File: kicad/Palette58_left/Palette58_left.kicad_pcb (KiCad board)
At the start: 2 copper layers, 145 x 127.8 mm, 124 parts, among them SW1 MSK12C02-HB, SW2 TS-1187A-B-A-B

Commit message: Add mounting holes
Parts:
- added REF**: MountingHole_3.2mm_M3_Pad_Via, MountingHole:MountingHole_3.2mm_M3_Pad_Via, F.Cu at (87.0, -82.0)
- added REF**: MountingHole_3.2mm_M3_Pad_Via, MountingHole:MountingHole_3.2mm_M3_Pad_Via, F.Cu at (100.4, 0.00)
- added REF**: MountingHole_3.2mm_M3_Pad_Via, MountingHole:MountingHole_3.2mm_M3_Pad_Via, F.Cu at (13.5, 7.50)
- added REF**: MountingHole_3.2mm_M3_Pad_Via, MountingHole:MountingHole_3.2mm_M3_Pad_Via, F.Cu at (23.0, -77.5)
- LED1, LED10, LED11, LED12, LED13, LED14, LED15, LED16, LED17, LED18, LED19, LED2, LED20, LED21, LED22, LED23, LED24, LED25, LED26, LED27, LED28, LED29, LED3, LED4, LED5, LED6, LED7, LED8, LED9: value XINGLIGHTXL-1615RGBC-WS2812B -> (none); footprint LED_SMD:XINGLIGHT XL-1615RGBC-WS2812B -> WS2812B
- R1: footprint Resistor_SMD:R_0402_1005Metric -> Resistor
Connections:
- LED1 pad 1: VCC -> (no net)
- LED1 pad 2: Net-(LED1-DOUT) -> GND
- LED1 pad 3: GND -> (no net)
- LED1 pad 4: Net-(LED1-DIN) -> VCC
- LED10 pad 1: VCC -> (no net)
- LED10 pad 2: Net-(LED10-DOUT) -> GND
- LED10 pad 3: GND -> (no net)
- LED10 pad 4: Net-(LED10-DIN) -> VCC
- LED11 pad 1: VCC -> (no net)
- LED11 pad 2: Net-(LED11-DOUT) -> GND
- LED11 pad 3: GND -> (no net)
- LED11 pad 4: Net-(LED11-DIN) -> VCC
- LED12 pad 1: VCC -> (no net)
- LED12 pad 2: Net-(LED12-DOUT) -> GND
- LED12 pad 3: GND -> (no net)
- LED12 pad 4: Net-(LED12-DIN) -> VCC
- LED13 pad 1: VCC -> (no net)
- LED13 pad 2: Net-(LED13-DOUT) -> GND
- LED13 pad 3: GND -> (no net)
- LED13 pad 4: Net-(LED13-DIN) -> VCC
- LED14 pad 1: VCC -> (no net)
- LED14 pad 2: Net-(LED10-DIN) -> GND
- LED14 pad 3: GND -> (no net)
- LED14 pad 4: Net-(LED14-DIN) -> VCC
- LED15 pad 1: VCC -> (no net)
- LED15 pad 2: Net-(LED15-DOUT) -> GND
- LED15 pad 3: GND -> (no net)
- LED15 pad 4: Net-(LED11-DOUT) -> VCC
- LED16 pad 1: VCC -> (no net)
- LED16 pad 2: Net-(LED12-DIN) -> GND
- LED16 pad 3: GND -> (no net)
- LED16 pad 4: Net-(LED16-DIN) -> VCC
- LED17 pad 1: VCC -> (no net)
- LED17 pad 2: Net-(LED17-DOUT) -> GND
- LED17 pad 3: GND -> (no net)
- LED17 pad 4: Net-(LED13-DOUT) -> VCC
- LED18 pad 1: VCC -> (no net)
- LED18 pad 2: Net-(LED14-DIN) -> GND
- LED18 pad 3: GND -> (no net)
- LED18 pad 4: Net-(LED18-DIN) -> VCC
- LED19 pad 1: VCC -> (no net)
- LED19 pad 2: Net-(LED19-DOUT) -> GND
- LED19 pad 3: GND -> (no net)
- LED19 pad 4: Net-(LED15-DOUT) -> VCC
- LED2 pad 1: VCC -> (no net)
- LED2 pad 2: Net-(LED1-DIN) -> GND
- LED2 pad 3: GND -> (no net)
- LED2 pad 4: Net-(LED2-DIN) -> VCC
- LED20 pad 1: VCC -> (no net)
- LED20 pad 2: Net-(LED16-DIN) -> GND
- LED20 pad 3: GND -> (no net)
- LED20 pad 4: Net-(LED20-DIN) -> VCC
- LED21 pad 1: VCC -> (no net)
- LED21 pad 2: Net-(LED21-DOUT) -> GND
- LED21 pad 3: GND -> (no net)
- LED21 pad 4: Net-(LED17-DOUT) -> VCC
- LED22 pad 1: VCC -> (no net)
- LED22 pad 2: Net-(LED18-DIN) -> GND
- LED22 pad 3: GND -> (no net)
- LED22 pad 4: Net-(LED22-DIN) -> VCC
- LED23 pad 1: VCC -> (no net)
- LED23 pad 2: Net-(LED22-DIN) -> GND
- LED23 pad 3: GND -> (no net)
- LED23 pad 4: Net-(LED19-DOUT) -> VCC
- LED24 pad 1: VCC -> (no net)
- LED24 pad 2: Net-(LED20-DIN) -> GND
- LED24 pad 3: GND -> (no net)
- LED24 pad 4: Net-(LED24-DIN) -> VCC
- LED25 pad 1: VCC -> (no net)
- LED25 pad 2: Net-(LED25-DOUT) -> GND
- LED25 pad 3: GND -> (no net)
- LED25 pad 4: Net-(LED21-DOUT) -> VCC
- LED26 pad 1: VCC -> (no net)
- LED26 pad 2: Net-(LED26-DOUT) -> GND
- LED26 pad 3: GND -> (no net)
- LED26 pad 4: Net-(LED25-DOUT) -> VCC
- LED27 pad 1: VCC -> (no net)
- LED27 pad 2: Net-(LED27-DOUT) -> GND
- LED27 pad 3: GND -> (no net)
- LED27 pad 4: Net-(LED26-DOUT) -> VCC
- LED28 pad 1: VCC -> (no net)
- LED28 pad 2: Net-(LED28-DOUT) -> GND
- LED28 pad 3: GND -> (no net)
- LED28 pad 4: Net-(LED27-DOUT) -> VCC
- LED29 pad 1: VCC -> (no net)
- LED29 pad 2: unconnected-(LED29-DOUT-Pad2) -> GND
- LED29 pad 3: GND -> (no net)
- LED29 pad 4: Net-(LED28-DOUT) -> VCC
- LED3 pad 1: VCC -> (no net)
- LED3 pad 2: Net-(LED3-DOUT) -> GND
- LED3 pad 3: GND -> (no net)
- LED3 pad 4: Net-(LED3-DIN) -> VCC
- LED4 pad 1: VCC -> (no net)
- LED4 pad 2: Net-(LED3-DIN) -> GND
- LED4 pad 3: GND -> (no net)
- LED4 pad 4: Net-(LED4-DIN) -> VCC
- LED5 pad 1: VCC -> (no net)
- LED5 pad 2: Net-(LED5-DOUT) -> GND
- LED5 pad 3: GND -> (no net)
- LED5 pad 4: Net-(LED1-DOUT) -> VCC
- LED6 pad 1: VCC -> (no net)
- LED6 pad 2: Net-(LED2-DIN) -> GND
- LED6 pad 3: GND -> (no net)
- LED6 pad 4: Net-(LED10-DOUT) -> VCC
- LED7 pad 1: VCC -> (no net)
- LED7 pad 2: Net-(LED11-DIN) -> GND
- LED7 pad 3: GND -> (no net)
- LED7 pad 4: Net-(LED3-DOUT) -> VCC
- LED8 pad 1: VCC -> (no net)
- LED8 pad 2: Net-(LED4-DIN) -> GND
- LED8 pad 3: GND -> (no net)
- LED8 pad 4: Net-(LED12-DOUT) -> VCC
- LED9 pad 1: VCC -> (no net)
- LED9 pad 2: Net-(LED13-DIN) -> GND
- LED9 pad 3: GND -> (no net)
- LED9 pad 4: Net-(LED5-DOUT) -> VCC
- R1 pad 1: Net-(LED24-DIN) -> (no net)
- R1 pad 2: P0.06 -> (no net)
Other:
- net class Default added: clearance 0.2, trace_width 0.25, via_dia 0.8, via_drill 0.4

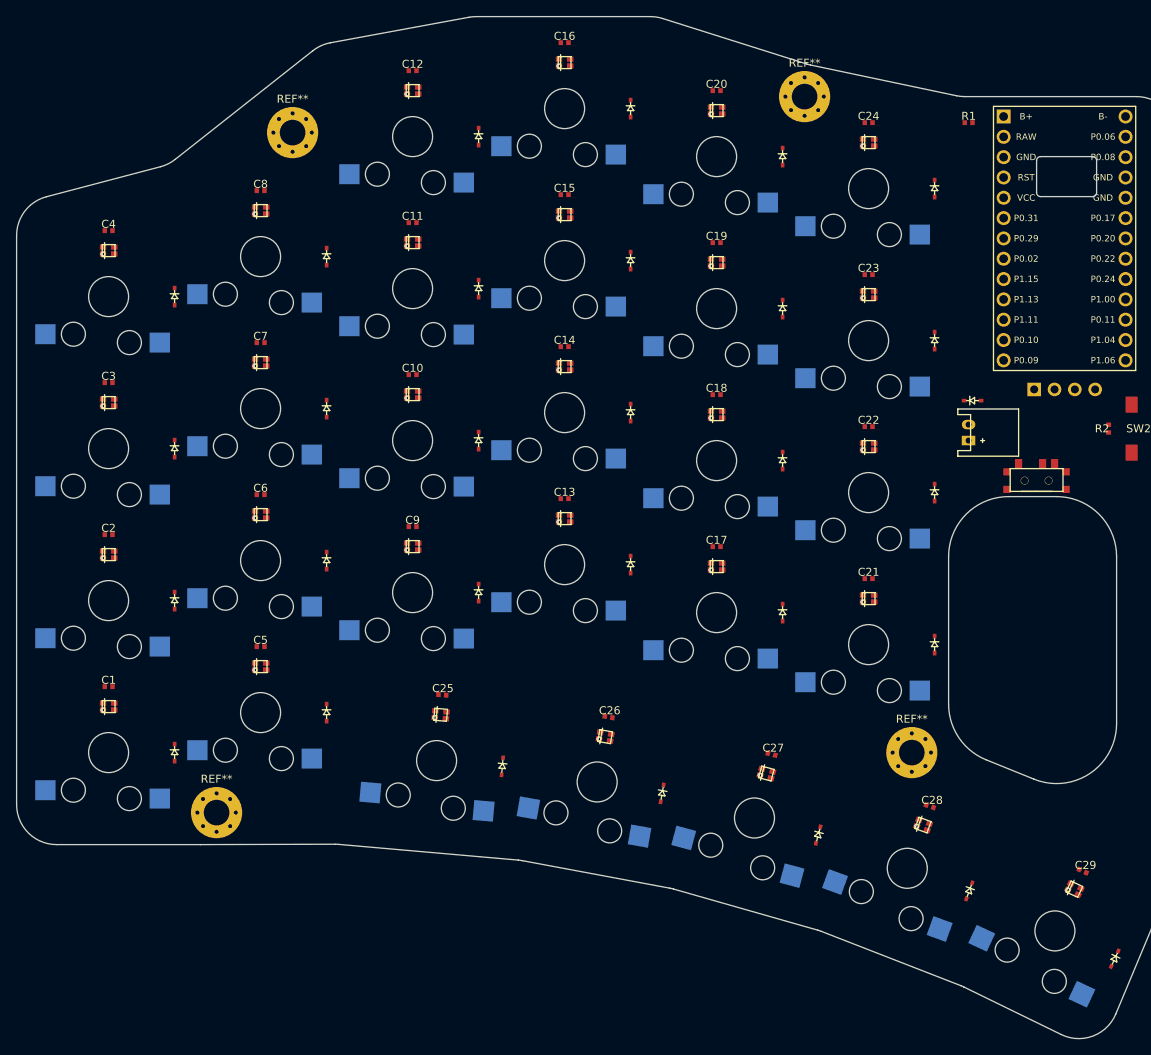
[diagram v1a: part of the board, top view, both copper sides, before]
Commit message: Add tooling holes
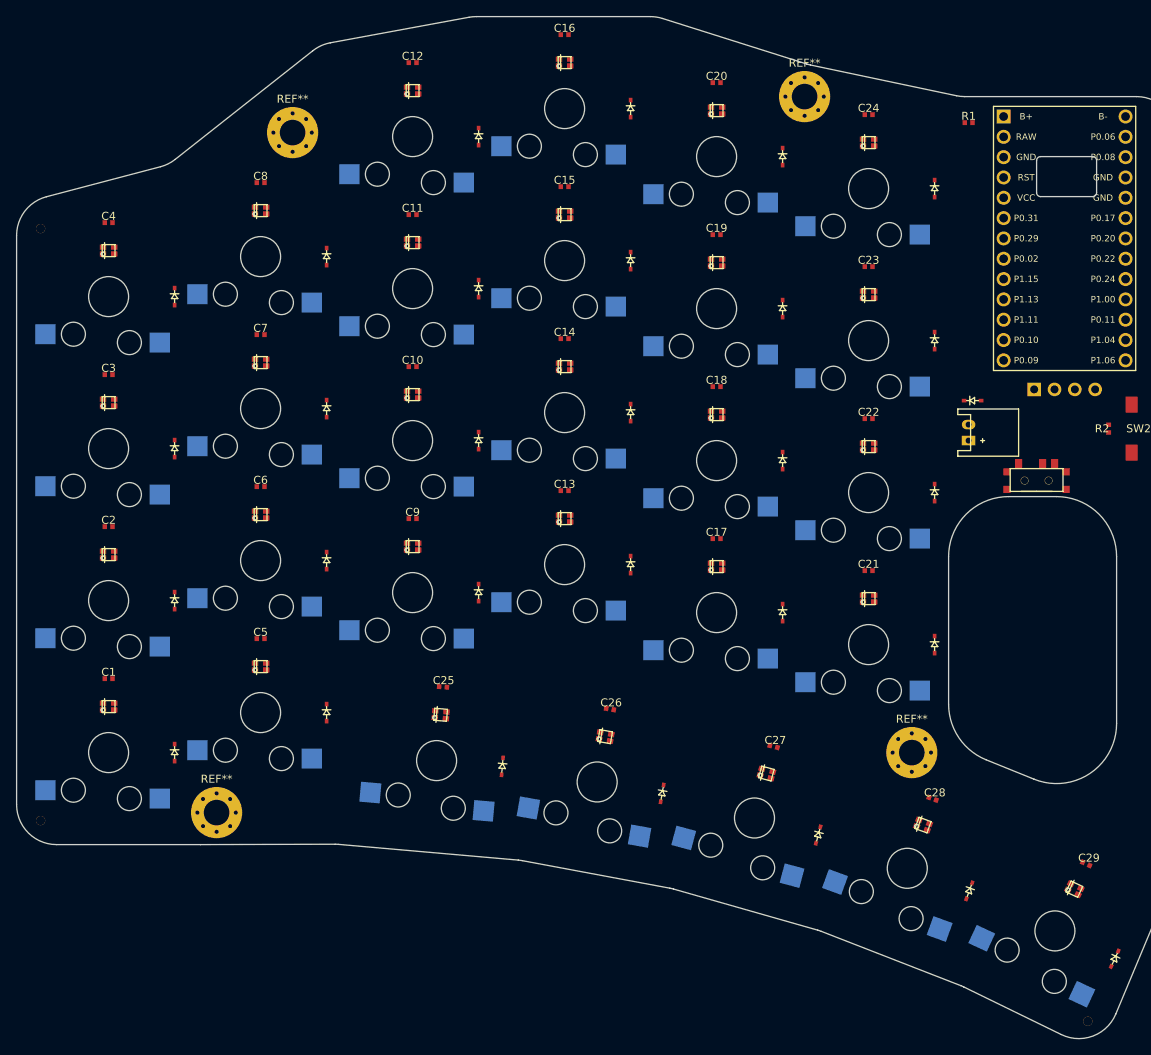
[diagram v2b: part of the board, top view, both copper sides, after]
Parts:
- added _34: , ToolingHole, F.Cu at (-8.50, -65.5)
- added _35: , ToolingHole, F.Cu at (-8.50, 8.50)
- added _36: , ToolingHole, F.Cu at (122.4, 33.6)
- moved C1 1.00 mm to (0.00, -9.25)
- moved C10 1.00 mm to (38.0, -48.2)
- moved C11 1.00 mm to (38.0, -67.2)
- moved C12 1.00 mm to (38.0, -86.2)
- moved C13 1.00 mm to (57.0, -32.8)
- moved C14 1.00 mm to (57.0, -51.8)
- moved C15 1.00 mm to (57.0, -70.8)
- moved C16 1.00 mm to (57.0, -89.8)
- moved C17 1.00 mm to (76.0, -26.8)
- moved C18 1.00 mm to (76.0, -45.8)
- moved C19 1.00 mm to (76.0, -64.8)
- moved C2 1.00 mm to (0.00, -28.2)
- moved C20 1.00 mm to (76.0, -83.8)
- moved C21 1.00 mm to (95.0, -22.8)
- moved C22 1.00 mm to (95.0, -41.8)
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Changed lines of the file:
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@@
     )
   (module Capacitor (layer F.Cu)
-      (at 0 -8.25 0)
+      (at 0 -9.25 0)
     (property "Reference" C1
       (at 0 -0.81)
@@
           )
   (module Capacitor (layer F.Cu)
-      (at 0 -27.25 0)
+      (at 0 -28.25 0)
     (property "Reference" C2
       (at 0 -0.81)
@@
           )
   (module Capacitor (layer F.Cu)
-      (at 0 -46.25 0)
+      (at 0 -47.25 0)
     (property "Reference" C3
       (at 0 -0.81)
@@
           )
   (module Capacitor (layer F.Cu)
-      (at 0 -65.25 0)
+      (at 0 -66.25 0)
     (property "Reference" C4
       (at 0 -0.81)
@@
           )
   (module Capacitor (layer F.Cu)
-      (at 19 -13.25 0)
+      (at 19 -14.25 0)
     (property "Reference" C5
       (at 0 -0.81)
@@
           )
   (module Capacitor (layer F.Cu)
-      (at 19 -32.25 0)
+      (at 19 -33.25 0)
     (property "Reference" C6
       (at 0 -0.81)
@@
           )
   (module Capacitor (layer F.Cu)
-      (at 19 -51.25 0)
+      (at 19 -52.25 0)
     (property "Reference" C7
       (at 0 -0.81)
@@
           )
   (module Capacitor (layer F.Cu)
-      (at 19 -70.25 0)
+      (at 19 -71.25 0)
     (property "Reference" C8
       (at 0 -0.81)
@@
           )
   (module Capacitor (layer F.Cu)
-      (at 38 -28.25 0)
+      (at 38 -29.25 0)
     (property "Reference" C9
       (at 0 -0.81)
@@
           )
   (module Capacitor (layer F.Cu)
-      (at 38 -47.25 0)
+      (at 38 -48.25 0)
     (property "Reference" C10
       (at 0 -0.81)
@@
           )
   (module Capacitor (layer F.Cu)
-      (at 38 -66.25 0)
+      (at 38 -67.25 0)
     (property "Reference" C11
       (at 0 -0.81)
@@
           )
   (module Capacitor (layer F.Cu)
-      (at 38 -85.25 0)
+      (at 38 -86.25 0)
     (property "Reference" C12
       (at 0 -0.81)
@@
           )
   (module Capacitor (layer F.Cu)
-      (at 57 -31.75 0)
+      (at 57 -32.75 0)
     (property "Reference" C13
       (at 0 -0.81)
@@
           )
   (module Capacitor (layer F.Cu)
-      (at 57 -50.75 0)
+      (at 57 -51.75 0)
     (property "Reference" C14
       (at 0 -0.81)
@@
           )
   (module Capacitor (layer F.Cu)
-      (at 57 -69.75 0)
+      (at 57 -70.75 0)
     (property "Reference" C15
       (at 0 -0.81)
@@
           )
   (module Capacitor (layer F.Cu)
-      (at 57 -88.75 0)
+      (at 57 -89.75 0)
     (property "Reference" C16
       (at 0 -0.81)
@@
           )
   (module Capacitor (layer F.Cu)
-      (at 76 -25.75 0)
+      (at 76 -26.75 0)
     (property "Reference" C17
       (at 0 -0.81)
@@
           )
   (module Capacitor (layer F.Cu)
-      (at 76 -44.75 0)
+      (at 76 -45.75 0)
     (property "Reference" C18
       (at 0 -0.81)
@@
           )
   (module Capacitor (layer F.Cu)
-      (at 76 -63.75 0)
+      (at 76 -64.75 0)
     (property "Reference" C19
       (at 0 -0.81)
@@
           )
   (module Capacitor (layer F.Cu)
-      (at 76 -82.75 0)
+      (at 76 -83.75 0)
     (property "Reference" C20
       (at 0 -0.81)
@@
           )
   (module Capacitor (layer F.Cu)
-      (at 95 -21.75 0)
+      (at 95 -22.75 0)
     (property "Reference" C21
       (at 0 -0.81)
@@
           )
   (module Capacitor (layer F.Cu)
-      (at 95 -40.75 0)
+      (at 95 -41.75 0)
     (property "Reference" C22
       (at 0 -0.81)
@@
           )
   (module Capacitor (layer F.Cu)
-      (at 95 -59.75 0)
+      (at 95 -60.75 0)
     (property "Reference" C23
       (at 0 -0.81)
@@
           )
   (module Capacitor (layer F.Cu)
-      (at 95 -78.75 0)
+      (at 95 -79.75 0)
     (property "Reference" C24
       (at 0 -0.81)
@@
           )
   (module Capacitor (layer F.Cu)
-      (at 41.7190349 -7.218606299999999 -5)
+      (at 41.8061906 -8.214801 -5)
     (property "Reference" C25
       (at 0 -0.81)
@@
           )
   (module Capacitor (layer F.Cu)
-      (at 62.5016283 -4.4551161 -10)
+      (at 62.6752764 -5.439923800000001 -10)
     (property "Reference" C26
       (at 0 -0.81)
@@
           )
   (module Capacitor (layer F.Cu)
-      (at 82.87160030000001 0.2047971999999989 -15)
+      (at 83.13041940000001 -0.761128600000001 -15)
     (property "Reference" C27
       (at 0 -0.81)
@@
           )
   (module Capacitor (layer F.Cu)
-      (at 102.65725640000001 6.7095129999999985 -20)
+      (at 102.99927650000001 5.769820399999999 -20)
     (property "Reference" C28
       (at 0 -0.81)
@@
           )
   (module Capacitor (layer F.Cu)
-      (at 121.77734350000001 14.810718199999997 -25)
+      (at 122.19996170000002 13.904410399999996 -25)
     (property "Reference" C29
       (at 0 -0.81)
@@
 		)
 	)
+  (module ToolingHole (layer F.Cu)
+    (at -8.5 -65.5 0)
+    (property "Reference" _34
+      (at 0 0)
+      (layer F.SilkS)
+      hide
+      (effects
+        (font
+          (size 1 1)
+          (thickness 0.15)
+        )
+      )
+    )
+		(property "Value" ""
+			(at 0 0)
+			(layer "F.Fab")
+      hide
+			(effects
+				(font
+					(size 1 1)
+					(thickness 0.15)
+				)
+			)
+		)
+    (pad "1" thru_hole circle
+      (at 0 0)
+      (size 1.152 1.152)
+      (drill 1.152)
+      (layers *.Cu *.SilkS *.Mask)
+			(remove_unused_layers no)
+			(zone_connect 2)
+    )
+  )
+  (module ToolingHole (layer F.Cu)
+    (at -8.5 8.5 0)
+    (property "Reference" _35
+      (at 0 0)
+      (layer F.SilkS)
+      hide
+      (effects
+        (font
+          (size 1 1)
+          (thickness 0.15)
+        )
+      )
+    )
+		(property "Value" ""
+			(at 0 0)
+			(layer "F.Fab")
+      hide
+			(effects
+				(font
+					(size 1 1)
+					(thickness 0.15)
+				)
+			)
+		)
+    (pad "1" thru_hole circle
+      (at 0 0)
+      (size 1.152 1.152)
+      (drill 1.152)
+      (layers *.Cu *.SilkS *.Mask)
+			(remove_unused_layers no)
+			(zone_connect 2)
+    )
+  )
+  (module ToolingHole (layer F.Cu)
+    (at 122.40210380000002 33.5836288 -25)
+    (property "Reference" _36
+      (at 0 0)
+      (layer F.SilkS)
+      hide
+      (effects
+        (font
+          (size 1 1)
+          (thickness 0.15)
+        )
+      )
+    )
+		(property "Value" ""
+			(at 0 0)
+			(layer "F.Fab")
+      hide
+			(effects
+				(font
+					(size 1 1)
+					(thickness 0.15)
+				)
+			)
+		)
+    (pad "1" thru_hole circle
+      (at 0 0)
+      (size 1.152 1.152)
+      (drill 1.152)
+      (layers *.Cu *.SilkS *.Mask)
+			(remove_unused_layers no)
+			(zone_connect 2)
+    )
+  )
   (gr_line (start 107.02060967499999 -82) (end 128.5 -82) (angle 90) (layer Edge.Cuts) (width 0.15))
 (gr_line (start 133.5 -77) (end 133.5 13.49672123132001) (angle 90) (layer Edge.Cuts) (width 0.15))
